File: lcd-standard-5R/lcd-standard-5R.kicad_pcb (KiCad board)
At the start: 4 copper layers, 137.4 x 82.6 mm, 161 parts, among them J1 USB_C_Receptacle_USB2.0_16P, J10 Conn_01x10_MountingPin, J2 SWD, J3 Conn_ARM_JTAG_SWD_10, J4 Micro_SD_Card_Det1, J5 Conn_01x06_MountingPin, J6 Conn_01x40_MountingPin, J7 Conn_01x02_MountingPin, J8 Serial, J9 AUX_IO, Q1 DMG3415, Q2 MMBT3904, Q3 MMBT3904, Q4 MMBT3904, SW1 SW_Push, SW2 SW_Push, SW3 BOOT0, SW4 RST, U1 USBLC6-2SC6, U2 AMS1117-3.3, U3 STM32H743ZITx, U4 MT48LC16M16A2P, U5 MT25Q, U6 CAT24C256, U7 XPT2046TS, U8 TPS61169, U9 MAX98357A, Y1 25MHz, Y2 32.768KHz

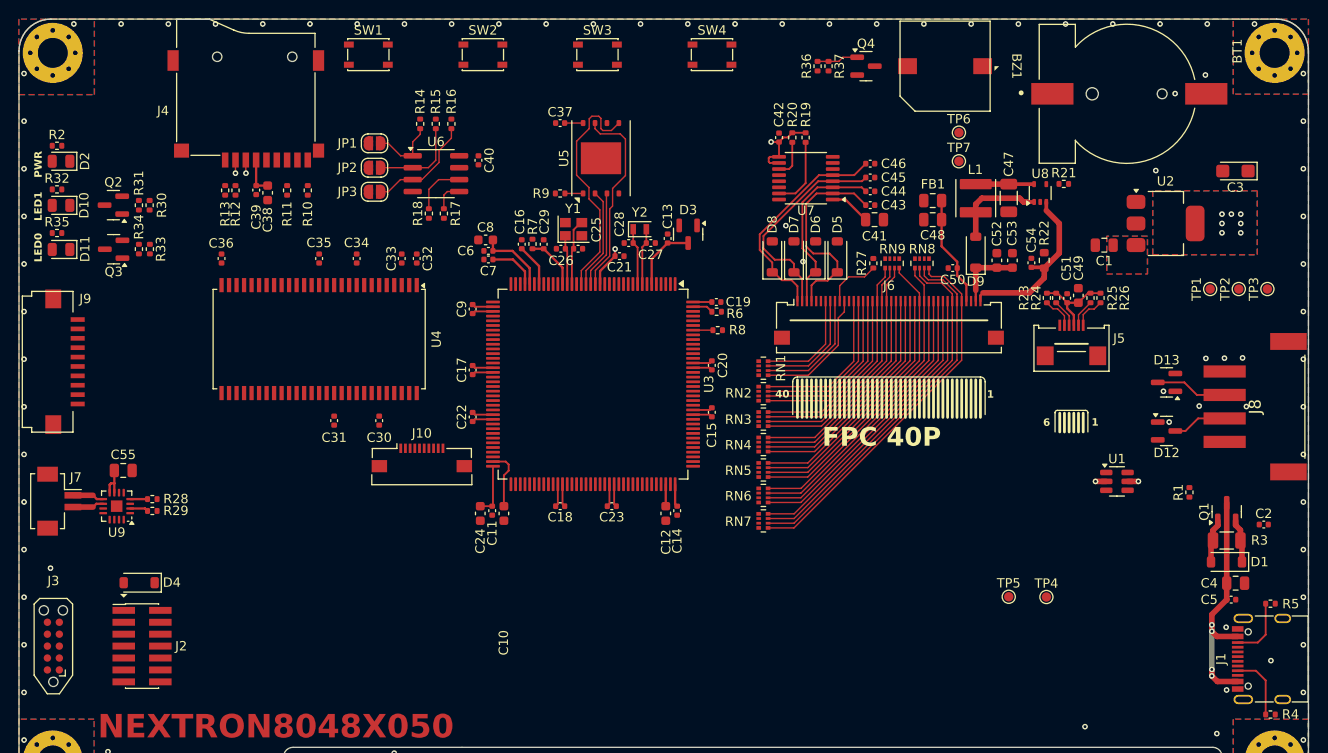
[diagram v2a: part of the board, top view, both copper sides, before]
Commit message: Change 10P CTP to omron type
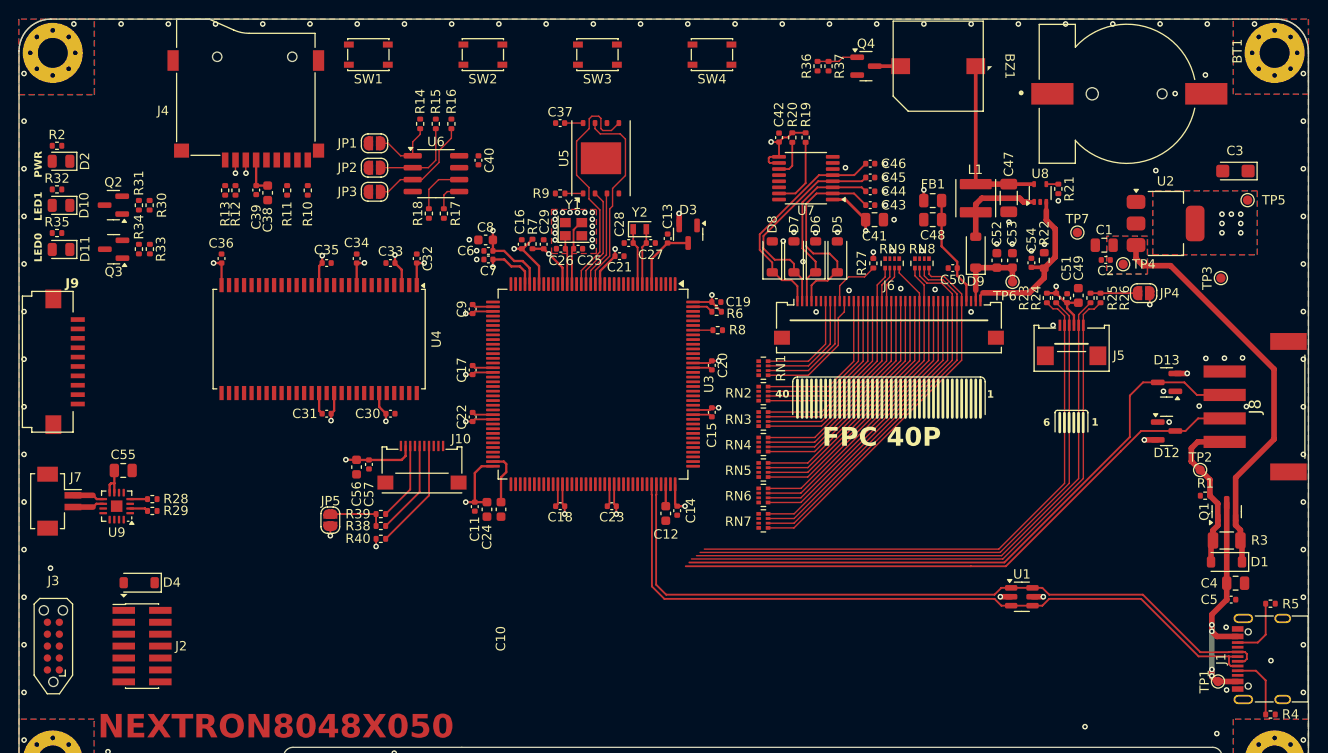
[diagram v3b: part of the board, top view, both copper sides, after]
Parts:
- added C56: 1u, Capacitor_SMD:C_0603_1608Metric, F.Cu at (112.4, 101.6)
- added C57: 100n, Capacitor_SMD:C_0402_1005Metric, F.Cu at (113.7, 101.4)
- added JP4: JMP, Jumper:SolderJumper-2_P1.3mm_Open_RoundedPad1.0x1.5mm, F.Cu at (196.3, 83.1)
- added JP5: JMP, Jumper:SolderJumper-2_P1.3mm_Open_RoundedPad1.0x1.5mm, F.Cu at (109.6, 107.3)
- added R38: 2K2, Resistor_SMD:R_0402_1005Metric, F.Cu at (115.0, 107.9)
- added R39: 2K2, Resistor_SMD:R_0402_1005Metric, F.Cu at (115.0, 106.7)
- added R40: 10K, Resistor_SMD:R_0402_1005Metric, F.Cu at (115.0, 109.3)
- J10: value Conn_01x10_MountingPin -> CTP_10P; footprint Connector_FFC-FPC:Molex_54548-1071_1x10-1MP_P0.5mm_Horizontal -> Connector_FPC:Conn_FPC_10P_0.5mm_OMRON_XF2M-1015-1A
- J5: value Conn_01x06_MountingPin -> CTP_6P
- J6: value Conn_01x40_MountingPin -> LCD_40P
- moved TP5 49.3 mm to (207.3, 73.2)
- moved TP1 41.8 mm to (204.2, 124.5)
- moved TP4 36.4 mm to (194.1, 80.0)
- moved C2 32.8 mm to (192.2, 79.6), turned to 180 degrees
- moved TP2 19.7 mm to (202.3, 102.0)
- moved TP6 16.9 mm to (182.3, 81.9)
- moved U1 15.9 mm to (183.3, 115.5)
- moved TP7 14.7 mm to (189.2, 76.7)
- moved TP3 5.09 mm to (204.5, 81.5)
- moved C11 1.90 mm to (125.0, 105.9)
- moved R1 1.71 mm to (202.8, 104.7), turned to 180 degrees
- moved C30 1.41 mm to (116.0, 96.0), turned to 0 degrees
- moved C33 1.29 mm to (116.0, 79.9), turned to 180 degrees
- moved J10 1.27 mm to (119.4, 99.4)
- moved C31 1.09 mm to (109.2, 96.0), turned to 180 degrees
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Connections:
- J10 pad 1: unconnected-(J10-Pin_1-Pad1) -> GND
- J10 pad 10: unconnected-(J10-Pin_10-Pad10) -> GND
- J10 pad 2: unconnected-(J10-Pin_2-Pad2) -> +3V3
- J10 pad 3: unconnected-(J10-Pin_3-Pad3) -> /DISPLAY/CTP_SCL
- J10 pad 4: unconnected-(J10-Pin_4-Pad4) -> GND
- J10 pad 5: unconnected-(J10-Pin_5-Pad5) -> /DISPLAY/CTP_SDA
- J10 pad 6: unconnected-(J10-Pin_6-Pad6) -> GND
- J10 pad 7: unconnected-(J10-Pin_7-Pad7) -> /DISPLAY/CTP_RST
- J10 pad 8: unconnected-(J10-Pin_8-Pad8) -> /DISPLAY/CTP_WAKE
- J10 pad 9: unconnected-(J10-Pin_9-Pad9) -> /DISPLAY/CTP_INT
- J10 pad MP: unconnected-(J10-MountPin-PadMP) -> GND
- R25 pad 1: +3V3 -> Net-(JP4-A)
- R26 pad 1: +3V3 -> Net-(JP4-A)
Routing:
- net /MCU/USB_D+: track 0.00 -> 79.0 mm
- net /MCU/USB_D-: track 0.00 -> 78.8 mm
- net /DISPLAY/CTP_SDA: track 2.93 -> 73.4 mm
- net /DISPLAY/CTP_SCL: track 3.50 -> 73.5 mm
- net /IO/SERIAL_RX: track 7.68 -> 68.1 mm
- net /DISPLAY/CTP_WAKE: track 2.97 -> 62.2 mm
- net /IO/SERIAL_TX: track 5.81 -> 64.0 mm
- net /DISPLAY/CTP_INT: track 3.47 -> 61.6 mm
- net +3V3: track 75.5 -> 128.5 mm, vias 9 -> 40
- net VDD: track 14.7 -> 66.1 mm
- net VEXT: track 4.72 -> 17.4 mm
- net /DISPLAY/CTP_RST: track 0.00 -> 11.8 mm
- net Net-(JP5-A): track 0.00 -> 6.14 mm
- net Net-(JP4-A): track 0.00 -> 5.01 mm
- net Net-(BZ1--): track 0.00 -> 2.76 mm
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
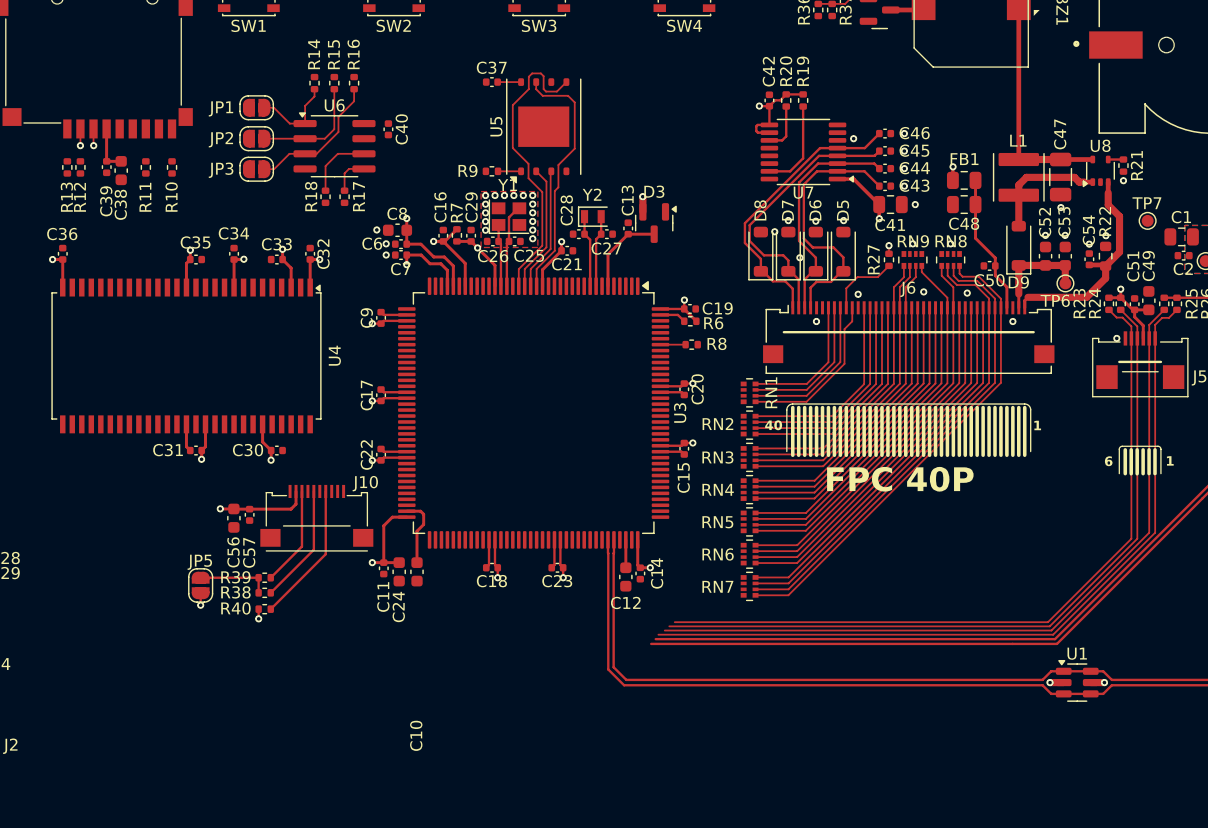
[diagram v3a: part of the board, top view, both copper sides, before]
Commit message: Finished SDRAM, LCD (need checkup with CubeIDE), RTP touch controll
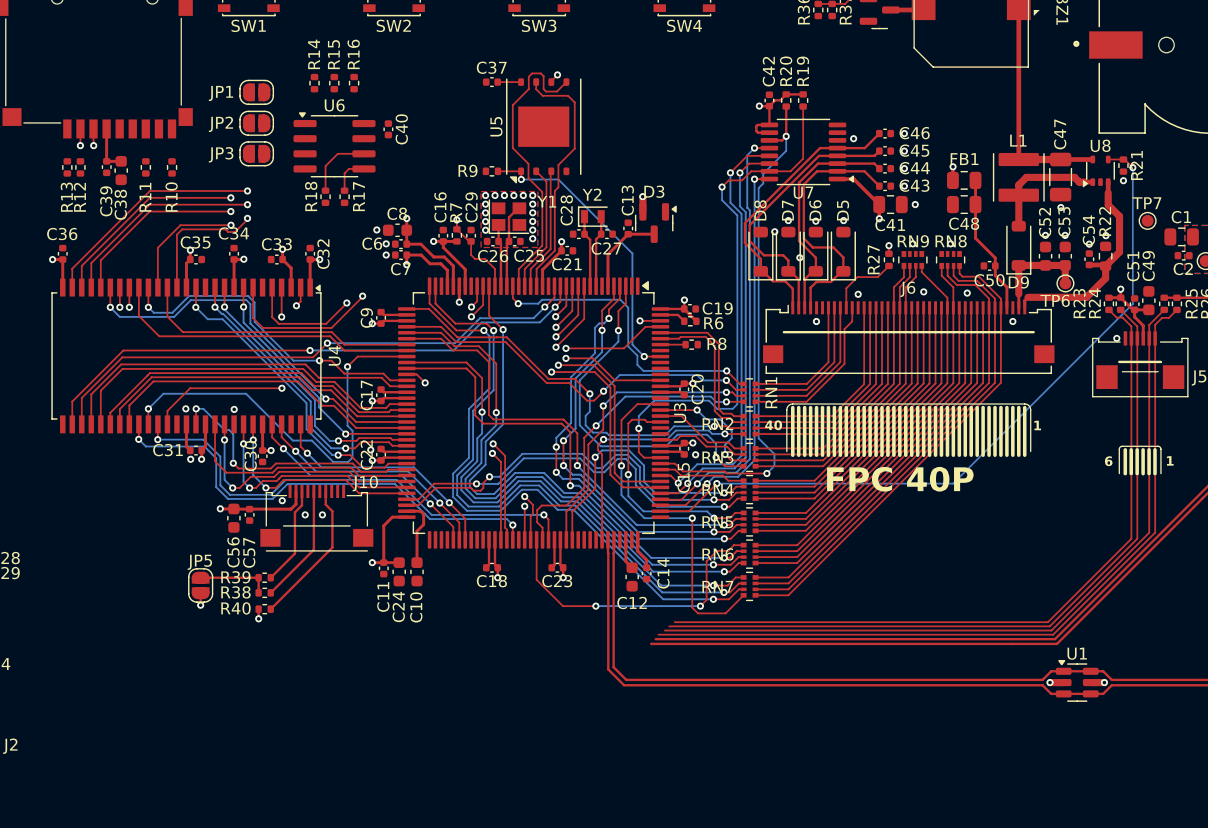
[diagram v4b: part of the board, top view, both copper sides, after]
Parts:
- C4: value 4u7 -> 4u7/0805
- RN8, RN9: value 10K -> 10K_Pack
- moved JP2 1.30 mm to (114.3, 68.5)
- moved JP3 1.30 mm to (114.3, 71.0)
- moved JP1 1.30 mm to (114.3, 65.9)
- moved C30 1.29 mm to (114.8, 96.4), turned to -90 degrees
- moved C14 0.53 mm to (147.1, 106.3)
- moved C12 0.53 mm to (145.9, 106.6)
- turned R7 to 90 degrees
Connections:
- net /MCU/I2S_CK renamed /MCU/I2S_CLK
- net /MCU/SDRAM_BA0 renamed /MEMORY_FMC/SDRAM_BA0
- net /MCU/SDRAM_BA1 renamed /MEMORY_FMC/SDRAM_BA1
- net /MCU/SDRAM_CKE renamed /MEMORY_FMC/SDRAM_CKE
- net /MCU/SDRAM_CLK renamed /MEMORY_FMC/SDRAM_CLK
- net /MCU/SDRAM_LDQM renamed /MEMORY_FMC/SDRAM_LDQM
- net /MCU/SDRAM_UDQM renamed /MEMORY_FMC/SDRAM_UDQM
- net /MCU/USB_D+ renamed /USB_POWER/D+
- net /MCU/USB_D- renamed /USB_POWER/D-
- net /MCU/~{SDRAM_CAS} renamed /MEMORY_FMC/~{SDRAM_CAS}
- net /MCU/~{SDRAM_CS} renamed /MEMORY_FMC/~{SDRAM_CS}
- net /MCU/~{SDRAM_RAS} renamed /MEMORY_FMC/~{SDRAM_RAS}
- net /MEMORY_SD_CARD/SD_DAT0 renamed /MCU/SD_D0
- net /MEMORY_SD_CARD/SD_DAT1 renamed /MCU/SD_D1
- net /MEMORY_SD_CARD/SD_DAT2 renamed /MCU/SD_D2
- net /MEMORY_SD_CARD/SD_DAT3 renamed /MCU/SD_D3
- J2 pad 13: /MCU/DBG_RX -> /MCU/ST_LINK_RX
- J2 pad 14: /MCU/DBG_TX -> /MCU/ST_LINK_TX
- U3 pad 1: /MCU/LCS_SPI_CLK -> /MCU/LED_0
- U3 pad 100: /MCU/LCD_TP_SCL -> /MEMORY_EEPROM/EE_SCL
- U3 pad 101: /MCU/LTDC_R5 -> /MCU/ST_LINK_TX
- U3 pad 102: /MCU/LTDC_B4 -> /DISPLAY/LCD_B4
- U3 pad 110: unconnected-(U3-PA15-Pad110) -> /DISPLAY/LCD_BLK
- U3 pad 111: unconnected-(U3-PC10-Pad111) -> /DISPLAY/RTP_CLK
- U3 pad 112: unconnected-(U3-PC11-Pad112) -> /DISPLAY/RTP_MISO
- U3 pad 113: unconnected-(U3-PC12-Pad113) -> /DISPLAY/RTP_MOSI
- U3 pad 116: unconnected-(U3-PD2-Pad116) -> /DISPLAY/RTP_BUSY
- U3 pad 117: /MCU/LTDC_G7 -> /DISPLAY/LCD_G7
- U3 pad 118: unconnected-(U3-PD4-Pad118) -> /DISPLAY/RTP_IRQ
- U3 pad 119: /MCU/DBG_USART_TX -> /DISPLAY/RTP_CS
- U3 pad 122: /MCU/DBG_USART_RX -> /DISPLAY/LCD_B2
- U3 pad 123: /MEMORY_SD_CARD/SD_CMD -> /MCU/BTN_1
- U3 pad 124: /MCU/EXT_RX -> /IO/SERIAL_TX
- U3 pad 125: /MCU/LTDC_G3 -> /DISPLAY/LCD_G3
- U3 pad 126: /MCU/LTDC_B3 -> /DISPLAY/LCD_B3
- U3 pad 127: /MCU/LED_0 -> /DISPLAY/LCD_B1
- U3 pad 128: /MCU/LED_1 -> /DISPLAY/LCD_R0
- U3 pad 129: /MCU/EXT_TX -> /IO/SERIAL_RX
- U3 pad 135: /MEMORY_SD_CARD/SD_DET -> /MCU/AUX_PWM
- U3 pad 137: /MCU/LCD_TP_RST -> /MCU/ST_LINK_RX
- U3 pad 139: /MCU/LTDC_B6 -> /DISPLAY/LCD_B6
- U3 pad 140: /MCU/LTDC_B7 -> /DISPLAY/LCD_B7
- U3 pad 2: /MCU/LCS_SPI_CS -> /MCU/LED_1
- U3 pad 26: /MCU/~{SDRAM_WE} -> /DISPLAY/LCD_R5
- U3 pad 28: /MCU/I2S_SD_MODE -> /MEMORY_SD_CARD/SD_DET
- U3 pad 3: /DISPLAY/LCD_RST -> /DISPLAY/LCD_B0
- U3 pad 34: /MCU/BTN0 -> /MEMORY_SD_CARD/SD_CMD
- U3 pad 35: /MCU/BTN1 -> /DISPLAY/LCD_R2
- U3 pad 36: unconnected-(U3-PA2-Pad36) -> /DISPLAY/LCD_R1
- U3 pad 37: /MCU/LTDC_B5 -> /DISPLAY/LCD_B5
- U3 pad 4: unconnected-(U3-PE5-Pad4) -> /DISPLAY/LCD_G0
- U3 pad 41: /MCU/LTDC_R4 -> /DISPLAY/LCD_R4
- U3 pad 42: /MCU/LTDC_G2 -> /DISPLAY/LCD_G2
- U3 pad 43: /DISPLAY/LCD_BLK -> /MEMORY_FMC/~{SDRAM_WE}
- U3 pad 46: /MCU/LTDC_R3 -> /DISPLAY/LCD_R3
- U3 pad 47: /MCU/LTDC_R6 -> /DISPLAY/LCD_R6
- U3 pad 5: /MCU/LCS_SPI_DAT -> /DISPLAY/LCD_G1
- U3 pad 69: /MCU/LTDC_G4 -> /DISPLAY/LCD_G4
- U3 pad 7: unconnected-(U3-PC13-Pad7) -> /MCU/BTN_0
- U3 pad 70: /MCU/LTDC_G5 -> /DISPLAY/LCD_G5
- U3 pad 80: unconnected-(U3-PD11-Pad80) -> /DISPLAY/CTP_INT
- U3 pad 81: /MCU/AUX_SCL -> /DISPLAY/CTP_SCL
- U3 pad 82: /MCU/AUX_SDA -> /DISPLAY/CTP_SDA
- U3 pad 88: unconnected-(U3-PG3-Pad88) -> /DISPLAY/CTP_WAKE
- U3 pad 91: /MCU/LTDC_R7 -> /DISPLAY/LCD_R7
- U3 pad 97: /MCU/LTDC_G6 -> /DISPLAY/LCD_G6
- U3 pad 98: /MCU/LCD_TP_INT -> /DISPLAY/CTP_RST
- U3 pad 99: /MCU/LCD_TP_SDA -> /MEMORY_EEPROM/EE_SDA
- U4 pad 16: /MCU/~{SDRAM_WE} -> /MEMORY_FMC/~{SDRAM_WE}
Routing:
- net /DISPLAY/LCD_BLK: track 1.28 -> 60.7 mm, vias 0 -> 2
- net /MCU/SDRAM_ADD3: track 0.00 -> 53.7 mm, vias 0 -> 2
- net /MCU/SDRAM_ADD2: track 0.00 -> 53.6 mm, vias 0 -> 2
- net /MCU/SDRAM_ADD1: track 0.00 -> 53.4 mm, vias 0 -> 2
- net /MCU/SDRAM_ADD0: track 0.00 -> 53.3 mm, vias 0 -> 2
- net /DISPLAY/LCD_R1: track 0.00 -> 52.2 mm, vias 0 -> 2
- net /MEMORY_FMC/~{SDRAM_CAS}: track 0.00 -> 51.8 mm, vias 0 -> 2
- net /DISPLAY/LCD_R2: track 0.00 -> 51.6 mm, vias 0 -> 2
- net /MEMORY_FMC/SDRAM_LDQM: track 0.00 -> 51.6 mm, vias 0 -> 2
- net /MEMORY_FMC/SDRAM_BA1: track 0.00 -> 50.4 mm, vias 0 -> 2
- net /MEMORY_FMC/SDRAM_BA0: track 0.00 -> 50.2 mm, vias 0 -> 2
- net /MCU/SDRAM_DQ3: track 0.00 -> 49.0 mm, vias 0 -> 2
- net /DISPLAY/LCD_R4: track 0.00 -> 48.2 mm, vias 0 -> 2
- net /MCU/SDRAM_ADD4: track 0.00 -> 47.7 mm, vias 0 -> 2
- net /MEMORY_FMC/SDRAM_UDQM: track 0.00 -> 46.9 mm, vias 0 -> 2
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
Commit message: Finsihed, need to touch up a bit
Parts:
- added C58: 100n, Capacitor_SMD:C_0402_1005Metric, F.Cu at (134.5, 56.8)
- added C59: 100n, Capacitor_SMD:C_0402_1005Metric, F.Cu at (146.8, 56.8)
- added R41: 10K, Resistor_SMD:R_0402_1005Metric, F.Cu at (133.1, 56.8)
- added R42: 10K, Resistor_SMD:R_0402_1005Metric, F.Cu at (145.5, 56.8)
- moved D12 5.28 mm to (197.3, 92.7)
- moved D13 5.28 mm to (197.3, 97.7), turned to 0 degrees
- moved R12 3.37 mm to (96.1, 72.2)
- moved TP4 1.60 mm to (195.7, 80.3)
- moved C13 1.47 mm to (147.0, 77.3)
- moved D3 1.47 mm to (149.2, 76.8)
- moved R13 0.93 mm to (97.5, 72.2)
- moved SW3 0.91 mm to (138.0, 56.8)
- moved SW4 0.91 mm to (150.2, 56.8)
- moved SW1 0.91 mm to (113.6, 56.8)
- moved SW2 0.91 mm to (125.8, 56.8)
- moved D4 0.33 mm to (89.2, 113.6)
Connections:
- BT1 pad P: VBAT -> VB
- J2 pad 12: /MCU/RESET -> /MCU/NRST
- J2 pad 8: /MCU/SWO -> unconnected-(J2-Pin_8-Pad8)
- J3 pad 10: /MCU/RESET -> /MCU/NRST
- J3 pad 6: /MCU/SWO -> unconnected-(J3-SWO/TDO-Pad6)
- SW3 pad 1: /IO/BOOT0 -> /IO/BTN_0
- SW3 pad 2: +3V3 -> GND
- SW4 pad 1: /IO/RESET -> /IO/BTN_1
- U3 pad 1: /MCU/LED_0 -> /IO/LED0
- U3 pad 100: /MEMORY_EEPROM/EE_SCL -> /DISPLAY/CTP_SCL
- U3 pad 123: /MCU/BTN_1 -> /IO/BTN_1
- U3 pad 135: /MCU/AUX_PWM -> /IO/BUZZER
- U3 pad 2: /MCU/LED_1 -> /IO/LED1
- U3 pad 29: /MCU/I2S_SDO -> /OUTPUT_SPEAKER/I2S2_SDO
- U3 pad 7: /MCU/BTN_0 -> /IO/BTN_0
- U3 pad 73: /MCU/I2S_WS -> /OUTPUT_SPEAKER/I2S2_WS
- U3 pad 74: /MCU/I2S_CLK -> /OUTPUT_SPEAKER/I2S2_CLK
- U3 pad 81: /DISPLAY/CTP_SCL -> /MEMORY_EEPROM/EE_SCL
- U3 pad 82: /DISPLAY/CTP_SDA -> /MEMORY_EEPROM/EE_SDA
- U3 pad 99: /MEMORY_EEPROM/EE_SDA -> /DISPLAY/CTP_SDA
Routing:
- net VDD: track 66.1 -> 240.6 mm, vias 0 -> 7
- net /MCU/NRST: track 7.49 -> 135.7 mm, vias 1 -> 4
- net /MCU/ST_LINK_RX: track 0.00 -> 99.9 mm, vias 0 -> 2
- net /MCU/SWCLK: track 0.00 -> 95.2 mm, vias 0 -> 4
- net /OUTPUT_SPEAKER/I2S2_SDO: track 0.00 -> 84.3 mm, vias 0 -> 2
- net /MCU/SWDIO: track 0.00 -> 80.9 mm, vias 0 -> 4
- net /MCU/SD_D0: track 0.00 -> 72.8 mm, vias 0 -> 2
- net /MCU/SD_D1: track 0.00 -> 70.5 mm, vias 0 -> 2
- net /MCU/BOOT0: track 2.11 -> 71.7 mm, vias 0 -> 2
- net /MCU/ST_LINK_TX: track 0.00 -> 69.0 mm
- net /IO/LED1: track 0.00 -> 68.8 mm, vias 0 -> 2
- net /MEMORY_SD_CARD/SD_CMD: track 1.41 -> 70.1 mm, vias 1 -> 2
- net /IO/LED0: track 0.00 -> 67.7 mm, vias 0 -> 2
- net /MCU/SD_D3: track 1.41 -> 68.8 mm, vias 1 -> 0
- net /MCU/SD_D2: track 0.00 -> 62.8 mm
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- added copper zone on In1.Cu, net VDD
- added copper zone on In2.Cu, net VDD
